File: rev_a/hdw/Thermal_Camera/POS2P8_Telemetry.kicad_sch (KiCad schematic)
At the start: 0 parts

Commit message: duplicated telemetry for all rails, added random tweaks to logic levels of signals
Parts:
- added C501, C502, C503: 0.1uF, Capacitors_SMD:C_0603, symbol Custom_Library:C_Custom
- added DOC501, DOC502: TBD, symbol Custom_Library:I2C_Address
- added U502: MCP9804, Package_DFN_QFN:DFN-8-1EP_3x2mm_P0.5mm_EP1.3x1.5mm, symbol Sensor_Temperature:MCP9804_DFN
- added U?: INA231A, Custom Footprints Library:Texas_DSBGA-12_1.65x1.39mm_Layout3x4_P0.4mm, symbol Custom Library:INA231A
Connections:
- new net +2.8V: U?.D1 (BUS)
- new net +3.0V: C502.1, C503.1, U502.8 (V_{DD}), U?.B1 (VS)
- new net GND: C502.2, C503.2, U502.4 (GND), U502.9 (EP/GND), U?.C1 (GND)
- new net I2C_SCL: U502.2 (SCL), U?.A1 (SCL)
- new net I2C_SDA: U502.1 (SDA), U?.A2 (SDA)
- new net POS2P8_SNS+: C501.1, U?.D3 (IN+)
- new net POS2P8_SNS-: C501.2, U?.D2 (IN-)
- no-connect marks 0 -> 2
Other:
- note added: "Max Current = 3.1A RSHUNT = 0.02 Ohm CLSB = 9.46045E-05A CAL Register = 0x0A92"

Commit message: lots of schematic progress
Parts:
- C?: renamed from C502; footprint Capacitors_SMD:C_0603 -> (none); Digi-Key PN 1276-1935-1-ND -> (none); display_footprint 0603 -> (none)
- C?: renamed from C501; footprint Capacitors_SMD:C_0603 -> (none); Digi-Key PN 1276-1935-1-ND -> (none); display_footprint 0603 -> (none)
- C?: renamed from C503; footprint Capacitors_SMD:C_0603 -> (none); Digi-Key PN 1276-1935-1-ND -> (none); display_footprint 0603 -> (none)
- DOC?: renamed from DOC502; value TBD -> 0x1B
- DOC?: renamed from DOC501; value TBD -> 0x73
- gave numbers to parts that had none: 1
- renumbered U502 to U?
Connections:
- net +3.0V: now also U?.6 (A1), U?.7 (A0)
- net GND: now also U901.C3 (A1), U?.5 (A2)
- net I2C_SCL: now also U901.B3 (A0)

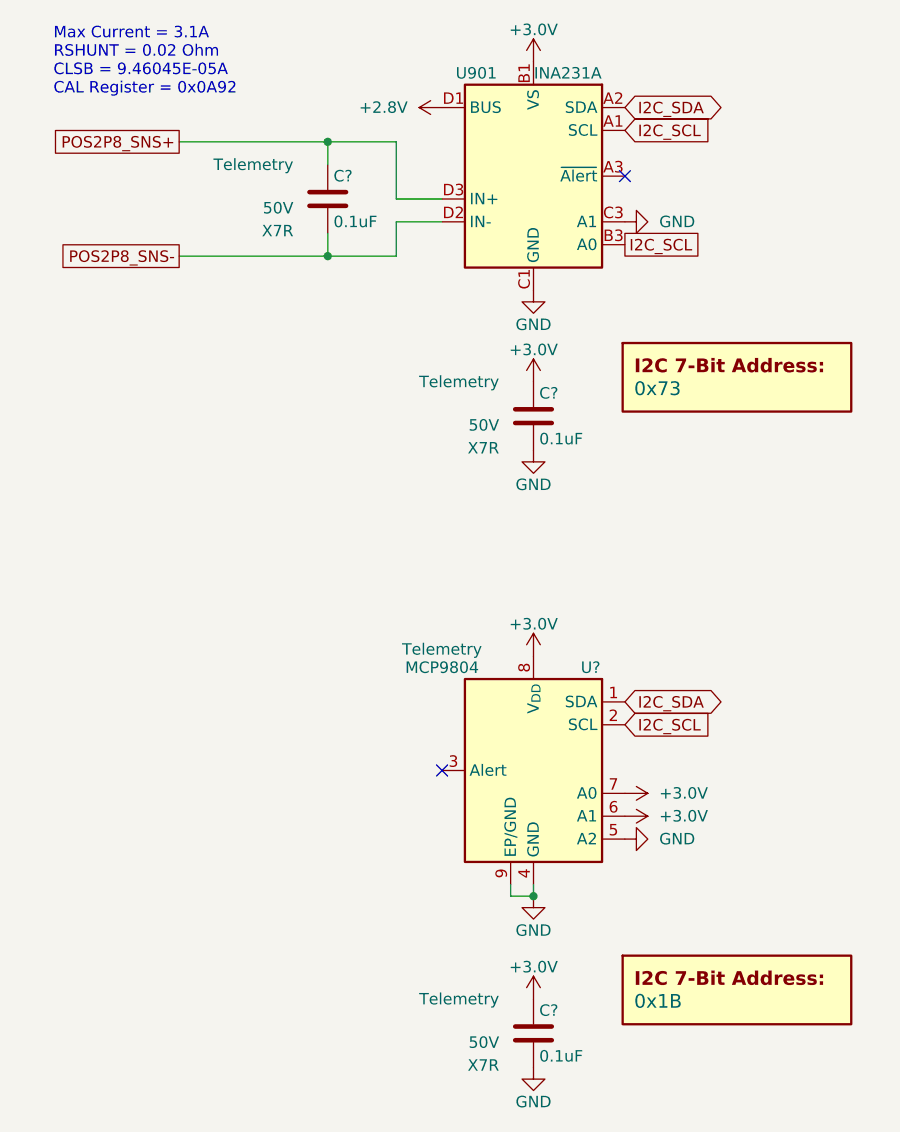
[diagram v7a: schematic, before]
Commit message: assigned a ton of footprints
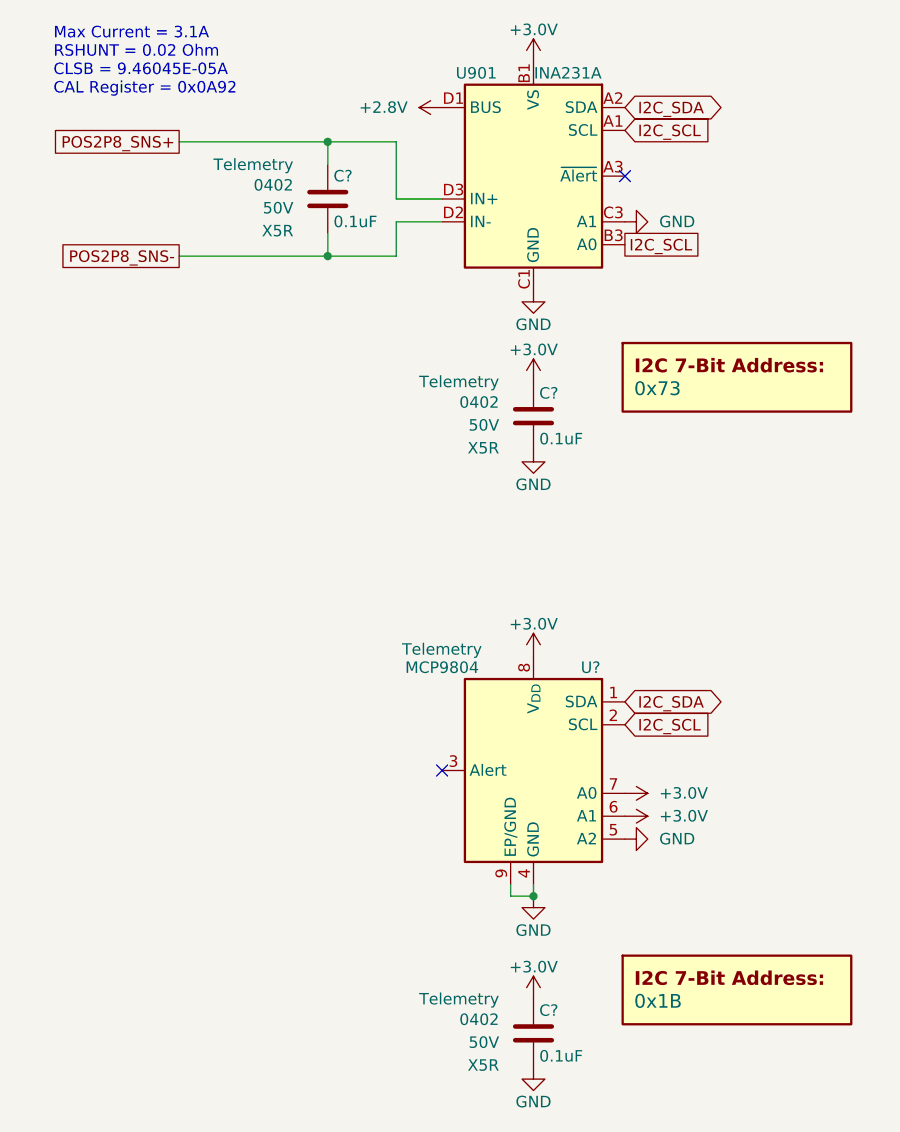
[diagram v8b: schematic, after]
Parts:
- C? (x3): footprint (none) -> Capacitors_SMD:C_0402; Dielectric X7R -> X5R; display_footprint (none) -> 0402
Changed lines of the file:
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@@
 			)
 		)
-		(property "Footprint" ""
+		(property "Footprint" "Capacitors_SMD:C_0402"
 			(at 136.8552 80.01 0)
 			(effects
@@
 			)
 		)
-		(property "display_footprint" ""
+		(property "display_footprint" "0402"
 			(at 132.08 74.676 0)
 			(effects
@@
 			)
 		)
-		(property "Dielectric" "X7R"
+		(property "Dielectric" "X5R"
 			(at 132.08 79.756 0)
 			(effects
@@
 			)
 		)
-		(property "Footprint" ""
+		(property "Footprint" "Capacitors_SMD:C_0402"
 			(at 113.9952 55.88 0)
 			(effects
@@
 			)
 		)
-		(property "display_footprint" ""
+		(property "display_footprint" "0402"
 			(at 109.22 50.546 0)
 			(effects
@@
 			)
 		)
-		(property "Dielectric" "X7R"
+		(property "Dielectric" "X5R"
 			(at 109.22 55.626 0)
 			(effects
@@
 			)
 		)
-		(property "Footprint" ""
+		(property "Footprint" "Capacitors_SMD:C_0402"
 			(at 136.8552 148.59 0)
 			(effects
@@
 			)
 		)
-		(property "display_footprint" ""
+		(property "display_footprint" "0402"
 			(at 132.08 143.256 0)
 			(effects
@@
 			)
 		)
-		(property "Dielectric" "X7R"
+		(property "Dielectric" "X5R"
 			(at 132.08 148.336 0)
 			(effects
